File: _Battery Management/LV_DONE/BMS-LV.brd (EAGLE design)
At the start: 94.8 x 65.8 mm, 120 parts, among them J1 M1x5, J2 M1x4, J3 M1x4, J4 M1x4, J5 M1x2, J6 MX150L, J7 M2770166, J8 M1x5, J9 M80022232081-2, K1 ADJ14024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

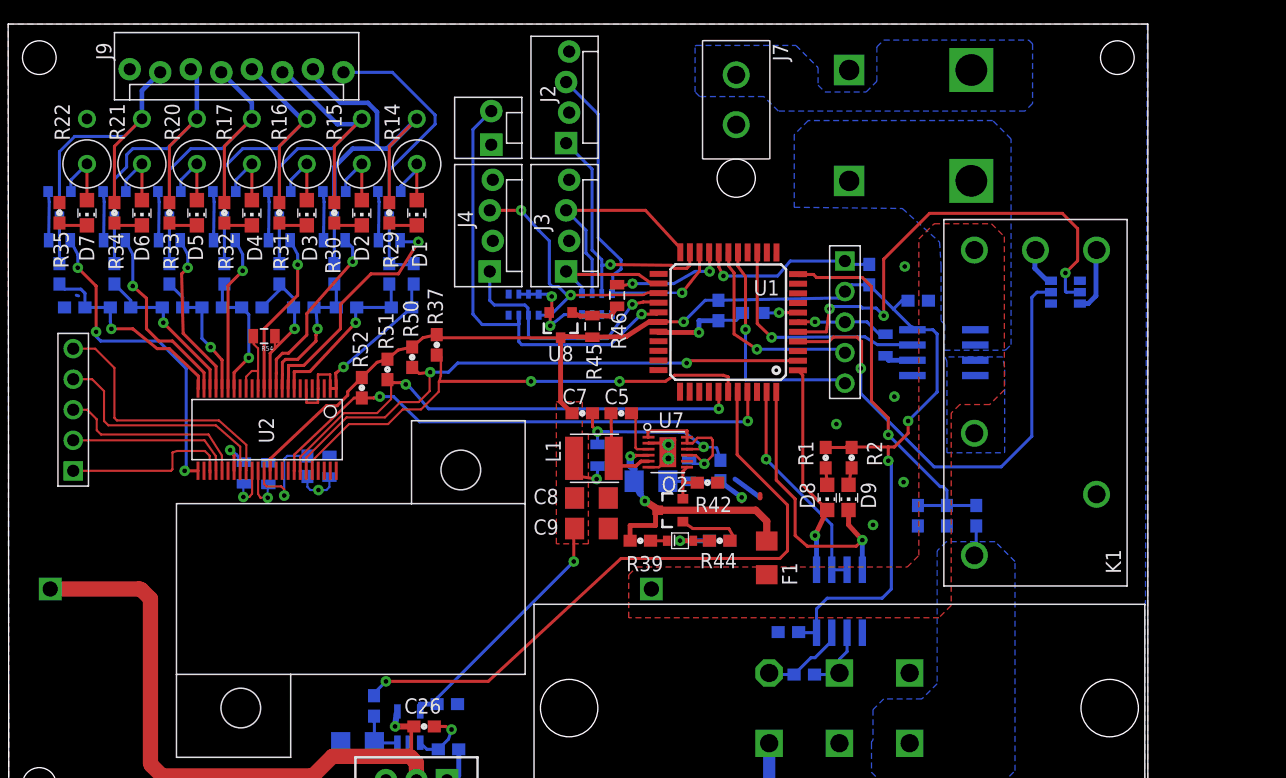
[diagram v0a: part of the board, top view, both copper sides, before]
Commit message: 
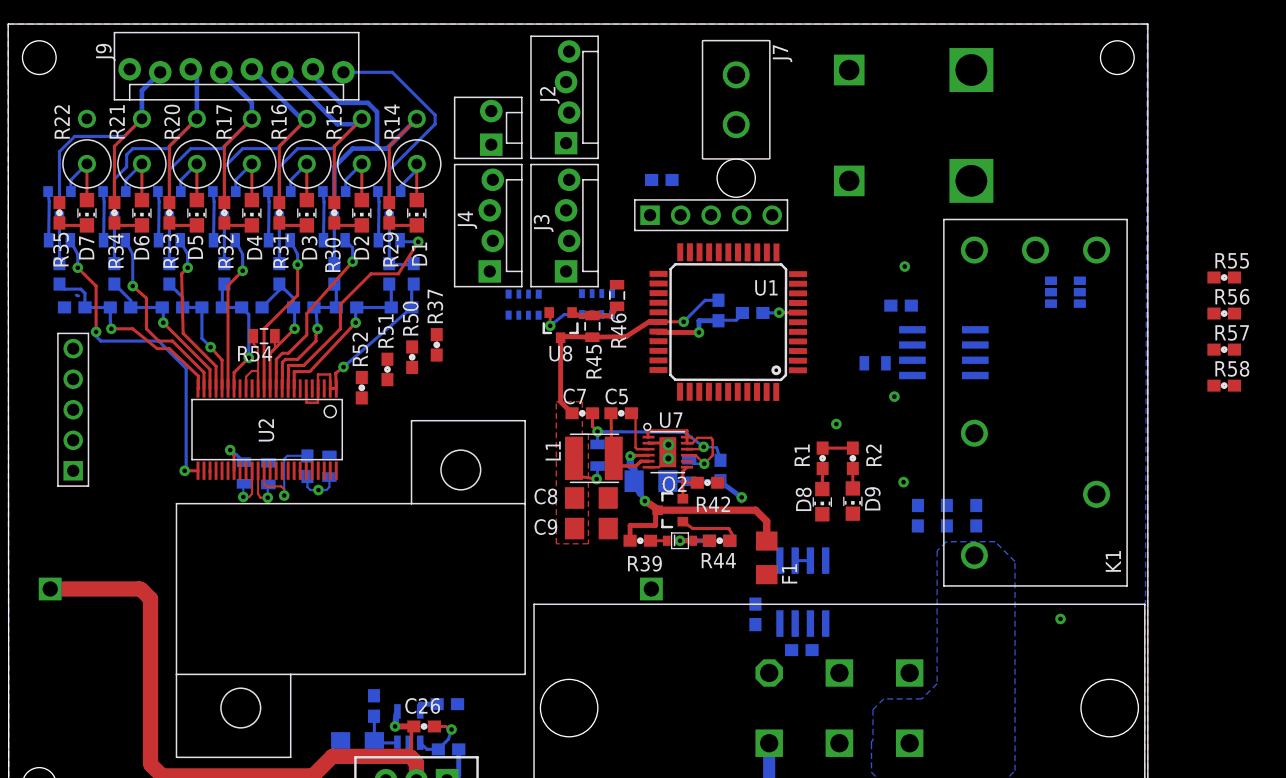
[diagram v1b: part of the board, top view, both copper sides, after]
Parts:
- added R55, R56: 1k, FSAE Electric:0603
- added R57, R58: 10k, FSAE Electric:0603
- moved R4 19.0 mm to (54.3, 52.8), turned to 180 degrees
- moved J1 14.2 mm to (58.4, 49.9), turned to 0 degrees
- moved U4 3.14 mm to (66.0, 18.5)
- moved C12 3.11 mm to (62.1, 16.7), turned to 90 degrees
- moved R3 2.04 mm to (66.0, 13.7)
- moved C2 1.75 mm to (72.1, 37.6), turned to 0 degrees
- moved C3 1.48 mm to (74.2, 42.4), turned to 0 degrees
- moved D8 0.54 mm to (67.7, 26.1)
- moved D9 0.47 mm to (70.2, 26.1)
- moved R1 0.26 mm to (67.7, 29.7)
- moved R2 0.11 mm to (70.2, 29.7)
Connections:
- new net N$19: R56.2, U1.4
- new net N$6: R55.2, U1.5
- net GND: now also R57.1
- net RSET: now also R58.2; no longer U1.5
- net SET: now also R55.1, R57.2; no longer U1.4
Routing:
- net +5V: track 138.9 -> 30.2 mm, vias 5 -> 2
- net CHARGECTRL: track 54.3 -> 0.00 mm, vias 1 -> 0
- net MOSI: track 48.3 -> 0.32 mm, vias 2 -> 0
- net CS: track 44.3 -> 0.00 mm, vias 2 -> 0
- net MISO: track 42.5 -> 0.00 mm, vias 2 -> 0
- net CLK: track 42.5 -> 0.10 mm, vias 2 -> 0
- net SET: track 41.1 -> 0.00 mm, vias 1 -> 0
- net RSET: track 39.0 -> 0.00 mm, vias 3 -> 0
- net TEMP7: track 37.5 -> 0.00 mm, vias 1 -> 0
- net VEXTERNAL: track 32.3 -> 0.38 mm, vias 1 -> 0
- net TEMP1: track 29.5 -> 0.00 mm, vias 1 -> 0
- net TX1: track 24.1 -> 0.00 mm, vias 1 -> 0
- net TEMP5: track 22.7 -> 0.00 mm, vias 2 -> 0
- net TEMP2: track 22.4 -> 0.00 mm, vias 1 -> 0
- net GPIO5: track 22.2 -> 0.00 mm
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- removed copper zone on layer 1, net BATTFUSED
- removed copper zone on layer 16, net BATTFUSED
- removed copper zone on layer 16, net N$15
- removed copper zone on layer 16, net N$5

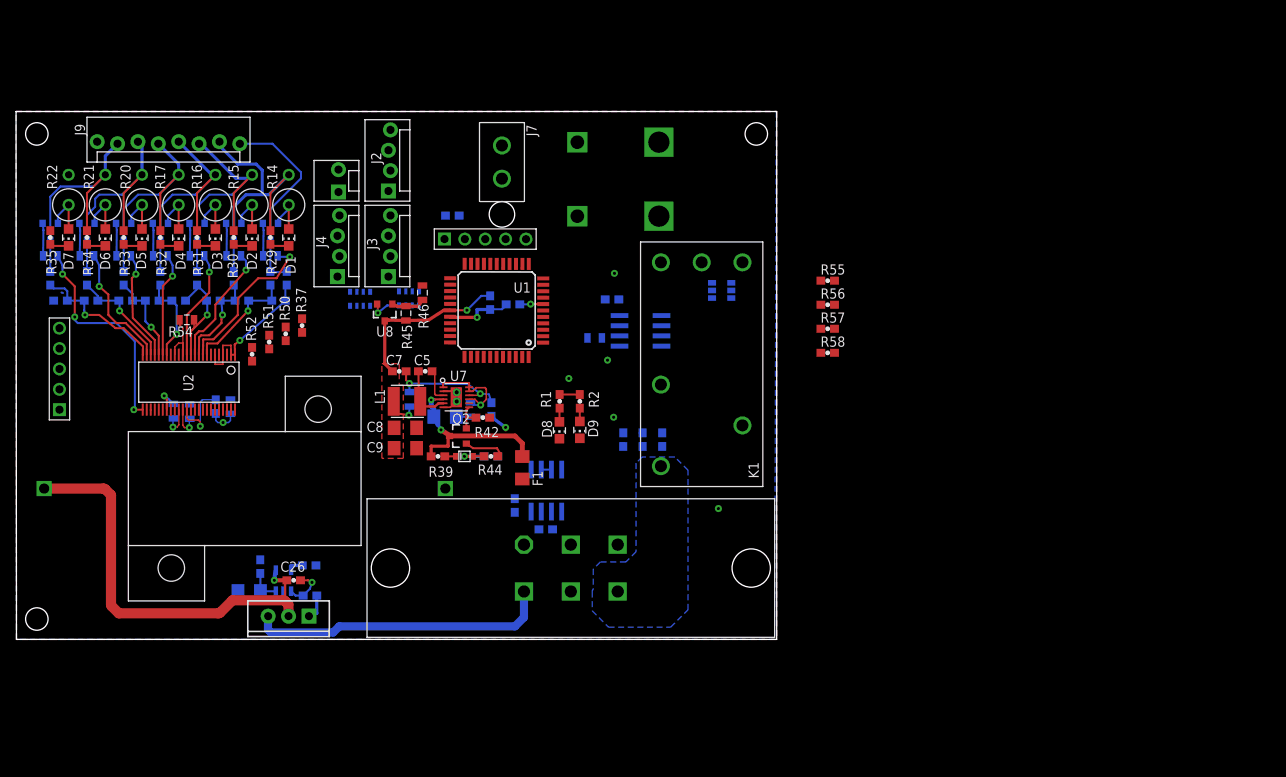
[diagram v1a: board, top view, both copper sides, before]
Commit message: 
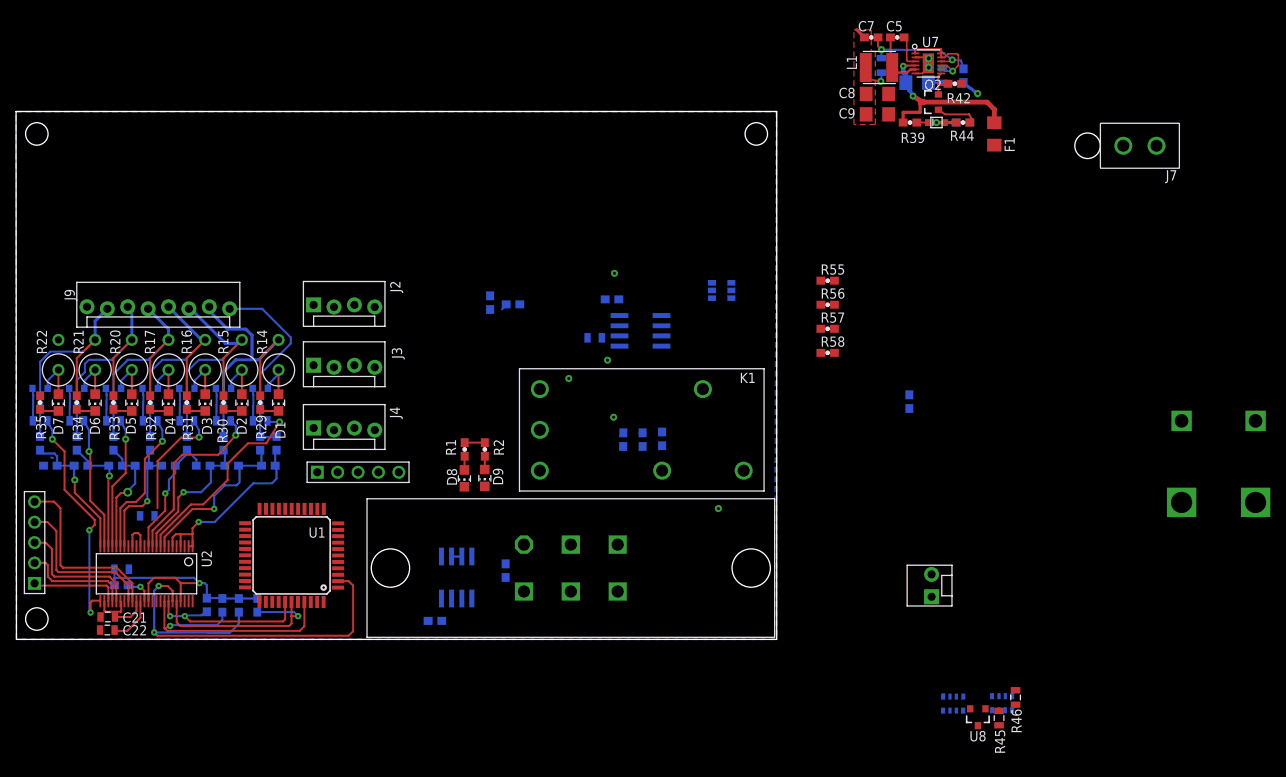
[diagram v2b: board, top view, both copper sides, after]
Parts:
- removed C24: 10uF, FSAE Electric:1206@1
- removed C25, C26: 0.1uF, FSAE Electric:0603
- removed Q3: BDX34C, FSAE Electric:TO-220
- removed R36: 1k, FSAE Electric:0603
- removed R38: 0.5, FSAE Electric:CHASSIS-MNT-RES-TE-HSA25
- removed R53: 100, FSAE Electric:0603
- removed U9: OPA344, FSAE Electric:SOT23-5
- moved J5 89.5 mm to (114.0, 6.71)
- moved U8 89.5 mm to (119.8, -9.65)
- moved R12 89.5 mm to (122.8, -7.98)
- moved R13 89.5 mm to (116.7, -7.98)
- moved R45 89.5 mm to (122.5, -9.80)
- moved R46 89.5 mm to (124.5, -7.24)
- moved F2 82.7 mm to (149.8, 22.1), turned to 180 degrees
- moved J7 79.5 mm to (140.0, 61.5), turned to 180 degrees
- moved C7 72.1 mm to (106.5, 75.0)
- moved Q2 72.1 mm to (113.9, 67.0)
- moved C4 72.1 mm to (112.2, 69.4)
- moved C5 72.1 mm to (109.8, 75.0)
- moved C6 72.1 mm to (115.4, 70.3)
- moved C8 72.1 mm to (107.3, 68.0)
- moved C9 72.1 mm to (107.3, 65.4)
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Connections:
- removed net +36V: J6.4, Q3.3
- removed net CHARGECTRL: R36.1, U1.40
- removed net N$14: C24.1, R36.2, U9.3
- removed net N$17: Q3.1, R53.2
- removed net N$21: C26.1, R53.1, U9.1
- removed net N$23: C26.2, Q3.2, R38.2, U9.4
- removed net VREG: C23.1, R47.2
- net +5V: now also C23.1, R47.2; no longer C25.1, U9.5
- net BATTFUSED: no longer R38.1
- net GND: now also J6.2; no longer C24.2, C25.2, U9.2
- net N$29: now also J6.4; no longer J6.2
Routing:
- net MOSI: track 0.32 -> 54.7 mm, vias 0 -> 2
- net N$23: track 53.0 -> 0.00 mm, vias 1 -> 0
- net +36V: track 37.7 -> 0.00 mm
- net CS: track 0.00 -> 32.7 mm, vias 0 -> 1
- net MISO: track 0.00 -> 26.1 mm, vias 0 -> 1
- net GPIO5: track 0.00 -> 22.8 mm
- net CLK: track 0.10 -> 21.8 mm, vias 0 -> 2
- net GPIO4: track 0.00 -> 19.8 mm
- net GPIO3: track 0.00 -> 16.4 mm
- net GPIO2: track 0.00 -> 13.7 mm
- net +5V: track 30.2 -> 42.8 mm
- net GPIO1: track 0.13 -> 11.1 mm
- net S8: track 15.4 -> 22.7 mm
- net N$2: track 14.5 -> 21.3 mm
- net N$78: track 6.74 -> 0.14 mm, vias 1 -> 0
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- removed copper zone on layer 16, net I/O

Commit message: 
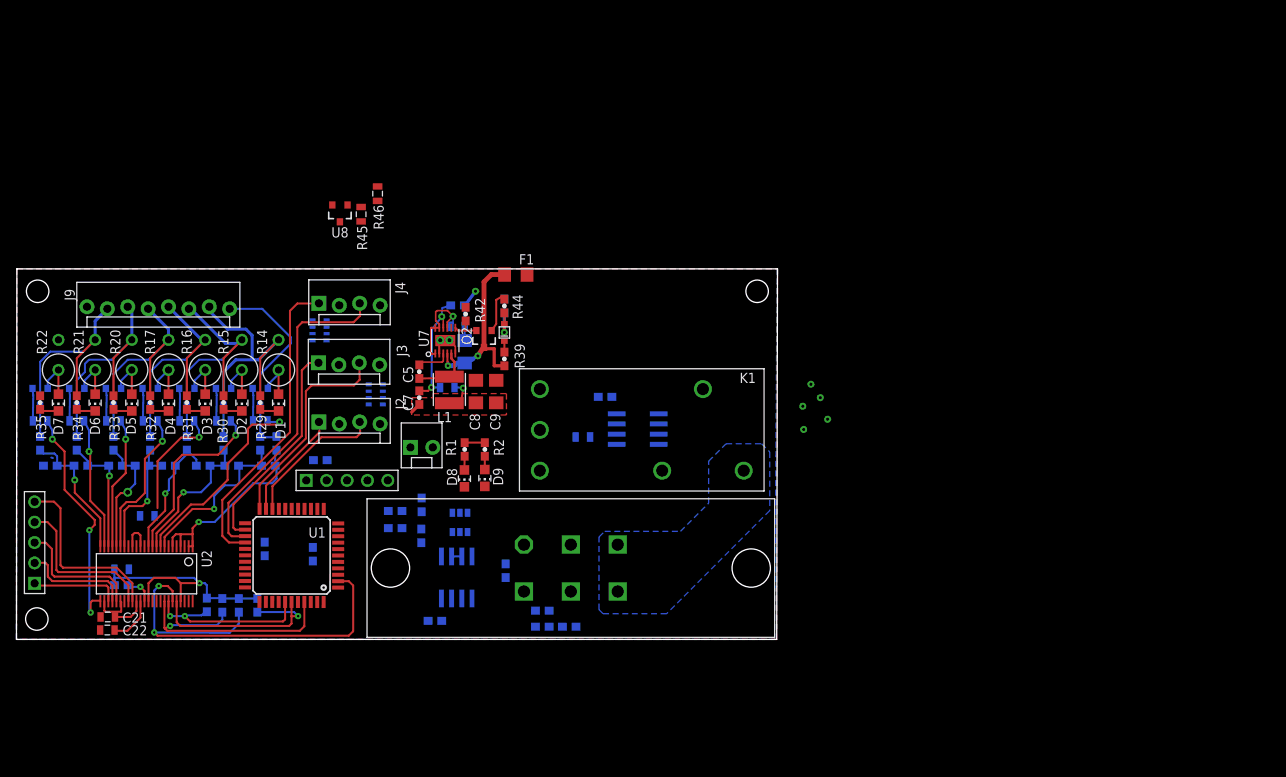
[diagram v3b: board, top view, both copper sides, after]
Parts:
- removed F2: FUSE CLIPS, FSAE Electric:FUSECLIP-3550
- removed J7: M2770166, FSAE Electric:1-770166-0
- moved R45 101.3 mm to (43.0, 53.0)
- moved R46 101.3 mm to (45.0, 55.5)
- moved U8 101.3 mm to (40.3, 53.1)
- moved R13 91.7 mm to (37.7, 38.5), turned to 270.1 degrees
- moved R12 87.0 mm to (44.8, 30.5), turned to 90 degrees
- moved R4 73.8 mm to (37.9, 22.3), turned to 180 degrees
- moved C5 72.7 mm to (50.2, 33.4), turned to 90 degrees
- moved C7 72.0 mm to (50.2, 30.1), turned to 90 degrees
- moved U7 69.4 mm to (53.4, 37.2), turned to 180 degrees
- moved R43 69.3 mm to (55.0, 41.6), turned to 0 degrees
- moved C6 68.0 mm to (55.0, 39.0), turned to 180 degrees
- moved R42 67.4 mm to (56.0, 40.5), turned to 270 degrees
- moved R41 67.4 mm to (53.7, 31.4), turned to 180 degrees
- moved L1 67.0 mm to (53.9, 31.1), turned to 270 degrees
- moved J5 65.8 mm to (50.5, 23.9), turned to 0 degrees
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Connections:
- removed net N$5: F2.1, J7.1
- net BATTFUSED: no longer F2.2
- net GND: now also R58.1; no longer J7.2
- net RSET: now also R56.1
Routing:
- net TEMP5: track 0.00 -> 41.4 mm
- net TEMP6: track 0.00 -> 38.7 mm
- net TEMP4: track 0.00 -> 27.8 mm
- net TEMP3: track 0.00 -> 26.5 mm
- net TEMP1: track 0.00 -> 17.9 mm
- net TEMP2: track 0.00 -> 13.6 mm
- net GND: track 19.2 -> 17.9 mm
- net S9: track 25.2 -> 25.9 mm
- added copper zone on layer 16, net I/O
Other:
- board size 94.8 x 65.8 mm -> 94.8 x 46.2 mm
- board text removed: "G. Synek"

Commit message: Fixing layout issues.
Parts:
- R12, R13: value 10k -> RN-4_10K
- moved C7 43.3 mm to (75.2, 65.5), turned to 0 degrees
- moved C5 42.8 mm to (78.4, 65.5), turned to 0 degrees
- moved U7 38.2 mm to (82.3, 62.3), turned to 90 degrees
- moved R41 38.2 mm to (76.5, 62.0), turned to 270 degrees
- moved L1 37.9 mm to (76.2, 61.7), turned to 180 degrees
- moved R43 37.0 mm to (86.7, 60.7), turned to 90 degrees
- moved R40 36.4 mm to (92.3, 59.8), turned to 180 degrees
- moved C6 36.3 mm to (84.1, 60.7), turned to 270 degrees
- moved R42 35.3 mm to (85.6, 59.7), turned to 180 degrees
- moved C4 34.7 mm to (80.9, 59.8), turned to 180 degrees
- moved R46 33.8 mm to (50.4, 22.2), turned to 180 degrees
- moved C8 33.3 mm to (76.0, 58.4), turned to 0 degrees
- moved Q2 31.4 mm to (82.6, 57.4), turned to 90 degrees
- moved R45 29.9 mm to (50.4, 24.0), turned to 180 degrees
- moved C9 29.8 mm to (76.0, 55.9), turned to 0 degrees
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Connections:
- net TEMP1: now also R12.1; no longer R12.4
- net TEMP2: now also R12.2; no longer R12.3
- net TEMP3: now also R12.4; no longer R12.2
- net TEMP4: now also R12.3; no longer R12.1
- net TEMP5: now also R13.2; no longer R13.1
- net TEMP6: now also R13.1; no longer R13.2
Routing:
- net VEXTERNAL: track 0.00 -> 44.3 mm, vias 0 -> 1
- net N$19: track 0.00 -> 41.2 mm, vias 0 -> 1
- net RX1: track 0.00 -> 39.8 mm, vias 0 -> 4
- net TX1: track 0.00 -> 39.2 mm, vias 0 -> 2
- net N$6: track 0.00 -> 36.7 mm, vias 0 -> 1
- net U4: track 1.27 -> 27.7 mm, vias 0 -> 1
- net RSET: track 0.00 -> 19.4 mm, vias 0 -> 2
- net N$24: track 22.9 -> 3.78 mm, vias 2 -> 1
- net N$33: track 0.00 -> 15.7 mm
- net TEMP6: track 38.7 -> 52.9 mm
- net N$39: track 0.00 -> 13.8 mm
- net +5V: track 42.8 -> 56.5 mm, vias 2 -> 3
- net N$10: track 0.00 -> 12.4 mm
- net N$29: track 0.00 -> 11.4 mm
- net TEMP7: track 0.00 -> 10.6 mm
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
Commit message: 
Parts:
- added D11: LED_AMBER, FSAE Electric:CHIP_LED0805
- added R/D, RX, TX: TPSMD, FSAE Electric:0603
- added R36: 1k, FSAE Electric:0603
- moved R42 33.2 mm to (63.0, 35.5), turned to 90 degrees
- moved R40 32.4 mm to (67.9, 38.6), flipped to the top, turned to 90 degrees
- moved R43 31.9 mm to (64.0, 38.3), turned to 0 degrees
- moved C6 30.7 mm to (66.6, 35.6), flipped to the top
- moved C7 29.2 mm to (60.1, 40.5), flipped to the bottom, turned to 180 degrees
- moved R41 28.8 mm to (60.1, 38.3), turned to 0 degrees
- moved U7 28.7 mm to (64.6, 39.7), turned to 0 degrees
- moved C5 26.7 mm to (62.8, 43.9), flipped to the bottom, turned to 270 degrees
- moved Q2 25.0 mm to (70.5, 35.6), turned to 180 degrees
- moved C8 24.3 mm to (59.5, 40.5)
- moved C9 24.3 mm to (59.5, 38.0)
- moved L1 24.3 mm to (59.8, 43.8)
- moved R44 23.2 mm to (70.5, 38.5), turned to 0 degrees
- moved C4 21.0 mm to (66.5, 44.6), flipped to the top, turned to 0 degrees
- moved D10 19.3 mm to (70.6, 40.4), turned to 180 degrees
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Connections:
- removed net VDD1: C10.1, U1.7
- new net N$14: R36.2, U1.30
- new net N$5: D11.A, R36.1
- net +5V: now also C10.1, U1.7
- net GND: now also D11.C
- net RX1: now also RX.1, RX.2
- net TX1: now also TX.1, TX.2
- net U4: now also R/D.1, R/D.2
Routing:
- net +5V: track 56.5 -> 171.6 mm, vias 3 -> 10
- net TEMP7: track 10.6 -> 66.8 mm, vias 0 -> 1
- net ASENSE: track 0.00 -> 55.0 mm, vias 0 -> 1
- net BATTFUSED: track 0.00 -> 30.1 mm, vias 0 -> 2
- net U4: track 27.7 -> 57.8 mm, vias 1 -> 2
- net N$24: track 3.78 -> 29.3 mm, vias 1 -> 2
- net TFET: track 0.00 -> 20.4 mm
- net N$78: track 0.00 -> 17.2 mm, vias 0 -> 1
- net TX1: track 39.2 -> 53.5 mm
- net RX1: track 39.8 -> 50.7 mm
- net N$31: track 4.21 -> 14.2 mm
- net GND: track 17.9 -> 9.08 mm, vias 3 -> 34
- net N$66: track 15.7 -> 8.12 mm, vias 2 -> 1
- net N$36: track 7.16 -> 1.40 mm, vias 0 -> 1
- net VDD1: track 5.43 -> 0.00 mm, vias 1 -> 0
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- added copper zone on layer 16, net BATTFUSED
- added copper zone on layer 16, net N$15
- added copper zone on layer 1, net N$24
- added copper zone on layer 1, net N$36
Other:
- board text added: "D10"
